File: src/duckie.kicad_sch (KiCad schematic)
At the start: 6 parts, among them SW1 SW_Push

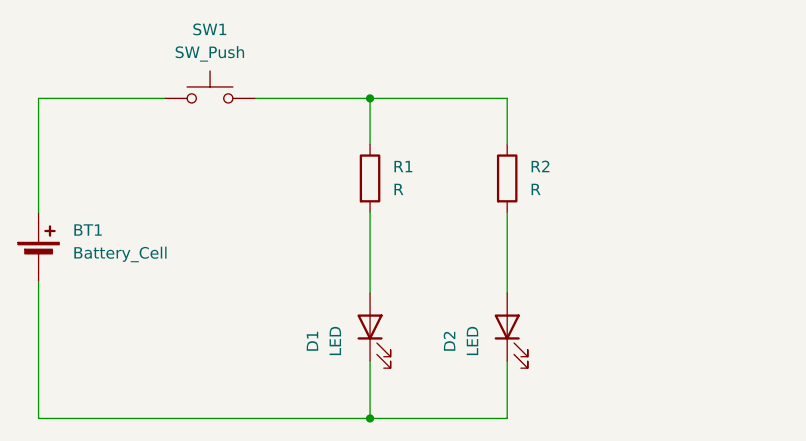
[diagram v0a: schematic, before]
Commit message: Updated PCB with buzz motor and potentiometer, and updated JOURNAL.md
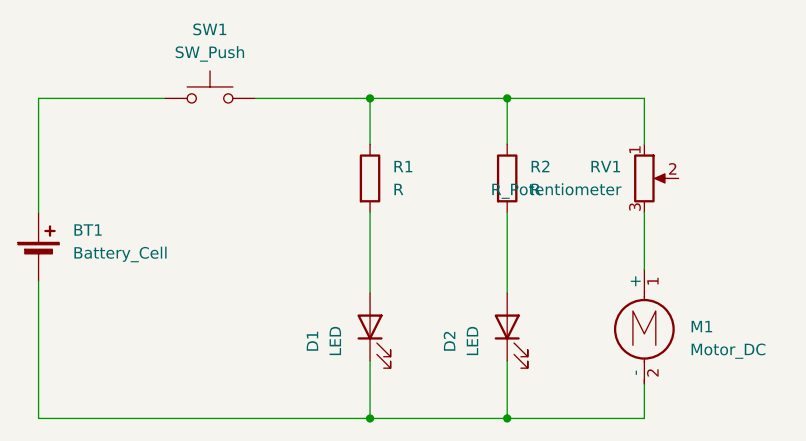
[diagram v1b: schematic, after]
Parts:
- added M1: Motor_DC, Connector_PinHeader_2.54mm:PinHeader_1x02_P2.54mm_Vertical, symbol Motor:Motor_DC
- added RV1: R_Potentiometer, Potentiometer_THT:Potentiometer_Vishay_T73YP_Vertical, symbol Device:R_Potentiometer
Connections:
- net at BT1.2 (-), D1.1 (K), D2.1 (K): now also M1.2 (-)
- net at R1.1, R2.1, SW1.2: now also RV1.1
- new net: M1.1 (+), RV1.3
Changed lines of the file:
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@@
 		(color 0 0 0 0)
 	)
+	(junction
+		(at 106.68 106.68)
+		(diameter 0)
+		(color 0 0 0 0)
+	)
+	(junction
+		(at 106.68 71.12)
+		(diameter 0)
+		(color 0 0 0 0)
+	)
 	(wire
 		(pts
@@
 	(wire
 		(pts
+			(xy 121.92 71.12) (xy 121.92 76.2)
+		)
+		(stroke
+			(width 0)
+			(type default)
+		)
+	)
+	(wire
+		(pts
 			(xy 54.61 106.68) (xy 54.61 91.44)
 		)
@@
 	(wire
 		(pts
+			(xy 121.92 106.68) (xy 121.92 102.87)
+		)
+		(stroke
+			(width 0)
+			(type default)
+		)
+	)
+	(wire
+		(pts
+			(xy 106.68 71.12) (xy 121.92 71.12)
+		)
+		(stroke
+			(width 0)
+			(type default)
+		)
+	)
+	(wire
+		(pts
 			(xy 54.61 83.82) (xy 54.61 71.12)
 		)
@@
 	(wire
 		(pts
+			(xy 121.92 83.82) (xy 121.92 90.17)
+		)
+		(stroke
+			(width 0)
+			(type default)
+		)
+	)
+	(wire
+		(pts
 			(xy 91.44 83.82) (xy 91.44 92.71)
 		)
@@
 		(pts
 			(xy 54.61 71.12) (xy 68.58 71.12)
+		)
+		(stroke
+			(width 0)
+			(type default)
+		)
+	)
+	(wire
+		(pts
+			(xy 106.68 106.68) (xy 121.92 106.68)
 		)
 		(stroke
@@
 	)
 	(symbol
+		(lib_id "Device:R_Potentiometer")
+		(at 121.92 80.01 0)
+		(unit 1)
+		(exclude_from_sim no)
+		(in_bom yes)
+		(on_board yes)
+		(dnp no)
+		(fields_autoplaced yes)
+		(property "Reference" "RV1"
+			(at 119.38 78.7399 0)
+			(effects
+				(font
+					(size 1.27 1.27)
+				)
+				(justify right)
+			)
+		)
+		(property "Value" "R_Potentiometer"
+			(at 119.38 81.2799 0)
+			(effects
+				(font
+					(size 1.27 1.27)
+				)
+				(justify right)
+			)
+		)
+		(property "Footprint" "Potentiometer_THT:Potentiometer_Vishay_T73YP_Vertical"
+			(at 121.92 80.01 0)
+			(effects
+				(font
+					(size 1.27 1.27)
+				)
+				(hide yes)
+			)
+		)
+		(property "Datasheet" "~"
+			(at 121.92 80.01 0)
+			(effects
+				(font
+					(size 1.27 1.27)
+				)
+				(hide yes)
+			)
+		)
+		(property "Description" "Potentiometer"
+			(at 121.92 80.01 0)
+			(effects
+				(font
+					(size 1.27 1.27)
+				)
+				(hide yes)
+			)
+		)
+		(pin "3"
+		)
+		(pin "1"
+		)
+		(pin "2"
+		)
+		(instances
+			(project ""
+				(path "/3e32be04-3dc8-4710-a4c2-b6beba23592e"
+					(reference "RV1")
+					(unit 1)
+				)
+			)
+		)
+	)
+	(symbol
 		(lib_id "Device:LED")
 		(at 91.44 96.52 90)
@@
 					(unit 1)
 				)
+			)
+		)
+	)
+	(symbol
+		(lib_id "Motor:Motor_DC")
+		(at 121.92 95.25 0)
+		(unit 1)
+		(exclude_from_sim no)
+		(in_bom yes)
+		(on_board yes)
+		(dnp no)
+		(fields_autoplaced yes)
+		(property "Reference" "M1"
+			(at 127 96.5199 0)
+			(effects
+				(font
+					(size 1.27 1.27)
+				)
+				(justify left)
+			)
+		)
+		(property "Value" "Motor_DC"
+			(at 127 99.0599 0)
+			(effects
+				(font
+					(size 1.27 1.27)
+				)
+				(justify left)
+			)
+		)
+		(property "Footprint" "Connector_PinHeader_2.54mm:PinHeader_1x02_P2.54mm_Vertical"
+			(at 121.92 97.536 0)
+			(effects
+				(font
+					(size 1.27 1.27)
+				)
+				(hide yes)
+			)
+		)
+		(property "Datasheet" "~"
+			(at 121.92 97.536 0)
+			(effects
+				(font
+					(size 1.27 1.27)
+				)
+				(hide yes)
+			)
+		)
+		(property "Description" "DC Motor"
+			(at 121.92 95.25 0)
+			(effects
+				(font
+					(size 1.27 1.27)
+				)
+				(hide yes)
+			)
+		)
+		(pin "2"
+		)
+		(pin "1"
+		)
+		(instances
+			(project ""
+				(path "/3e32be04-3dc8-4710-a4c2-b6beba23592e"
+					(reference "M1")
+					(unit 1)
+				)

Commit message: Changing potentiometer wiring
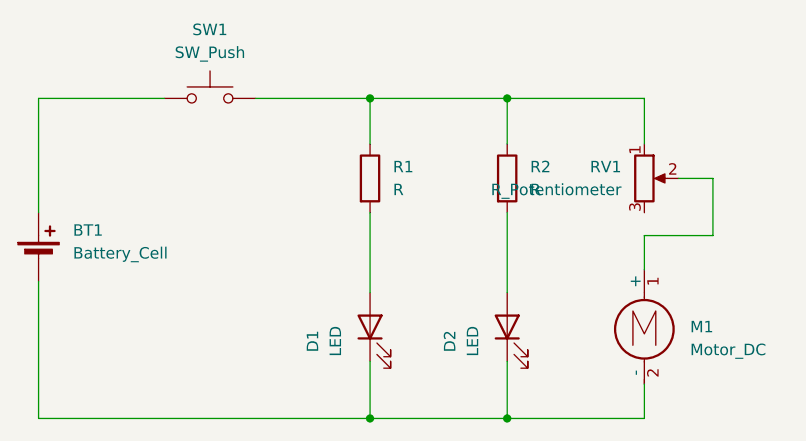
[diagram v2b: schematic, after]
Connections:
- net at RV1.2: now also M1.1 (+)
- net at RV1.3: no longer M1.1 (+)
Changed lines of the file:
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@@
+	(wire
+		(pts
+			(xy 129.54 80.01) (xy 129.54 86.36)
+		)
+		(stroke
+			(width 0)
+			(type default)
+		)
+	)
 	(wire
 		(pts
@@
 		(pts
 			(xy 121.92 106.68) (xy 121.92 102.87)
+		)
+		(stroke
+			(width 0)
+			(type default)
+		)
+	)
+	(wire
+		(pts
+			(xy 129.54 86.36) (xy 121.92 86.36)
 		)
 		(stroke
@@
 	(wire
 		(pts
-			(xy 121.92 83.82) (xy 121.92 90.17)
+			(xy 121.92 86.36) (xy 121.92 90.17)
 		)
 		(stroke
@@
 		)
 		(stroke
+			(width 0)
+			(type default)
+		)
+	)
+	(wire
+		(pts
+			(xy 125.73 80.01) (xy 129.54 80.01)
+		)
+		(stroke
